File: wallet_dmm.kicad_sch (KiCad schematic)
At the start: 16 parts, among them J1 Conn_01x04, SW1 REST_BUTTON, U1 TLC555xD, U2 STM32L051K8Tx

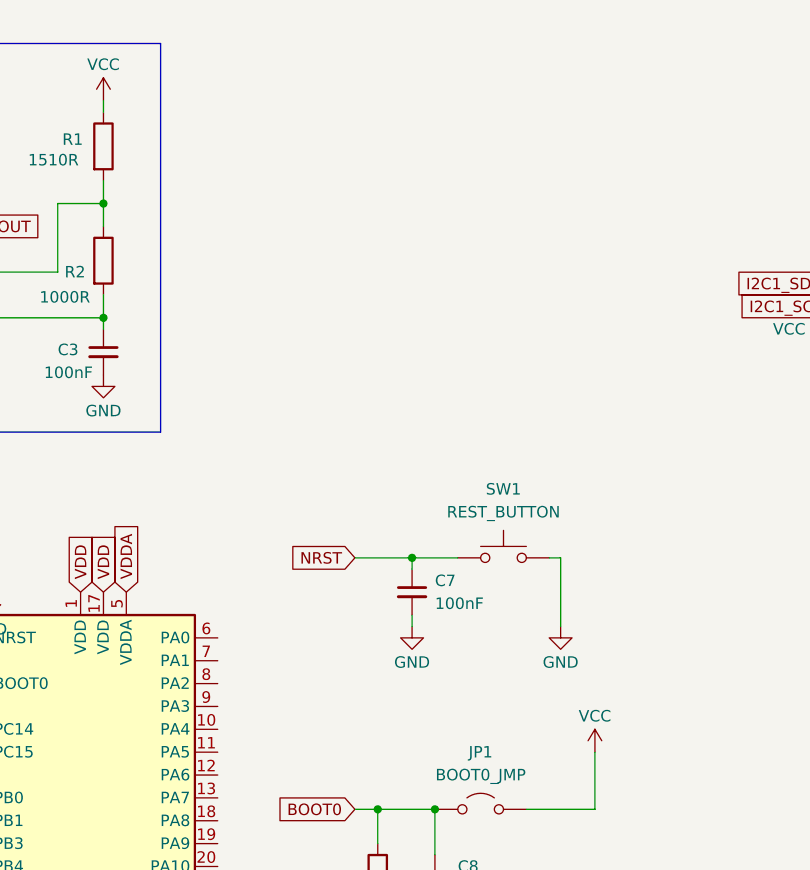
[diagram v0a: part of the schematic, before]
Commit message: Added temperature sensor to schematic and added .gitignore file.
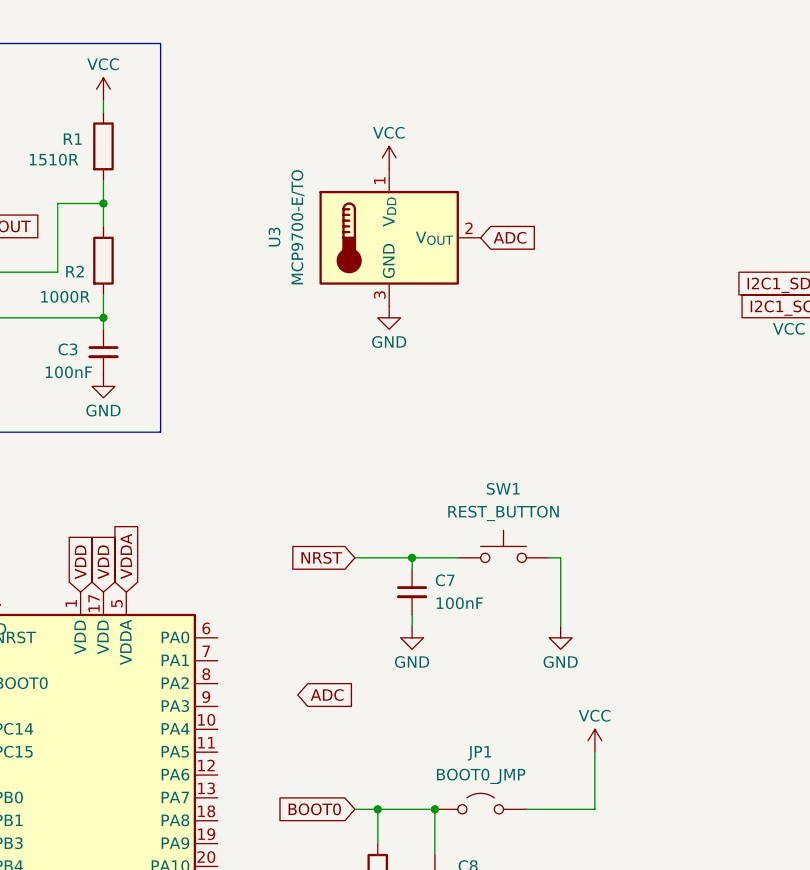
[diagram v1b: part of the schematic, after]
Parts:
- added U3: MCP9700-E/TO, footprints:TO-92_MC_MCH, symbol Sensor_Temperature:MCP9700Ax-ETT
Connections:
- net GND: now also U3.3 (GND)
- net VCC: now also U3.1 (V_{DD})
- new net ADC: U3.2 (V_{OUT})
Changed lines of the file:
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@@
+		)
+	)
+	(global_label "ADC"
+		(shape input)
+		(at 93.98 88.9 0)
+		(fields_autoplaced yes)
+		(effects
+			(font
+				(size 1.27 1.27)
+			)
+			(justify left)
+		)
+		(property "Intersheetrefs" "${INTERSHEET_REFS}"
+			(at 100.5938 88.9 0)
+			(effects
+				(font
+					(size 1.27 1.27)
+				)
+				(justify left)
+				(hide yes)
+			)
+		)
+	)
+	(global_label "ADC"
+		(shape input)
+		(at 114.3 38.1 0)
+		(fields_autoplaced yes)
+		(effects
+			(font
+				(size 1.27 1.27)
+			)
+			(justify left)
+		)
+		(property "Intersheetrefs" "${INTERSHEET_REFS}"
+			(at 120.9138 38.1 0)
+			(effects
+				(font
+					(size 1.27 1.27)
+				)
+				(justify left)
+				(hide yes)
+			)
 		)
 	)
@@
 	)
 	(symbol
+		(lib_id "power:VCC")
+		(at 104.14 30.48 0)
+		(mirror y)
+		(unit 1)
+		(exclude_from_sim no)
+		(in_bom yes)
+		(on_board yes)
+		(dnp no)
+		(property "Reference" "#PWR022"
+			(at 104.14 34.29 0)
+			(effects
+				(font
+					(size 1.27 1.27)
+				)
+				(hide yes)
+			)
+		)
+		(property "Value" "VCC"
+			(at 104.14 26.48 0)
+			(effects
+				(font
+					(size 1.27 1.27)
+				)
+			)
+		)
+		(property "Footprint" ""
+			(at 104.14 30.48 0)
+			(effects
+				(font
+					(size 1.27 1.27)
+				)
+				(hide yes)
+			)
+		)
+		(property "Datasheet" ""
+			(at 104.14 30.48 0)
+			(effects
+				(font
+					(size 1.27 1.27)
+				)
+				(hide yes)
+			)
+		)
+		(property "Description" "Power symbol creates a global label with name \"VCC\""
+			(at 104.14 30.48 0)
+			(effects
+				(font
+					(size 1.27 1.27)
+				)
+				(hide yes)
+			)
+		)
+		(pin "1"
+		)
+		(instances
+			(project "wallet_dmm"
+				(path "/2feb1339-af30-4942-92c0-e58400bfb20d"
+					(reference "#PWR022")
+					(unit 1)
+				)
+			)
+		)
+	)
+	(symbol
 		(lib_id "MCU_ST_STM32L0:STM32L051K8Tx")
 		(at 69.85 102.87 0)
@@
 	)
 	(symbol
+		(lib_id "Sensor_Temperature:MCP9700Ax-ETT")
+		(at 104.14 38.1 0)
+		(unit 1)
+		(exclude_from_sim no)
+		(in_bom yes)
+		(on_board yes)
+		(dnp no)
+		(property "Reference" "U3"
+			(at 91.44 36.83 90)
+			(effects
+				(font
+					(size 1.27 1.27)
+				)
+				(justify right)
+			)
+		)
+		(property "Value" "MCP9700-E/TO"
+			(at 93.98 30.48 90)
+			(effects
+				(font
+					(size 1.27 1.27)
+				)
+				(justify right)
+			)
+		)
+		(property "Footprint" "footprints:TO-92_MC_MCH"
+			(at 104.14 48.26 0)
+			(effects
+				(font
+					(size 1.27 1.27)
+				)
+				(hide yes)
+			)
+		)
+		(property "Datasheet" "http://ww1.microchip.com/downloads/en/devicedoc/20001942g.pdf"
+			(at 100.33 31.75 0)
+			(effects
+				(font
+					(size 1.27 1.27)
+				)
+				(hide yes)
+			)
+		)
+		(property "Description" "Low power, analog thermistor temperature sensor, ±2C accuracy, -40C to +125C, in SOT-23-3"
+			(at 104.14 38.1 0)
+			(effects
+				(font
+					(size 1.27 1.27)
+				)
+				(hide yes)
+			)
+		)
+		(pin "2"
+		)
+		(pin "3"
+		)
+		(pin "1"
+		)
+		(instances
+			(project "wallet_dmm"
+				(path "/2feb1339-af30-4942-92c0-e58400bfb20d"
+					(reference "U3")
+					(unit 1)
+				)
+			)
+		)
+	)
+	(symbol
 		(lib_id "Device:C_Small")
 		(at 34.29 80.01 0)
@@
 					(unit 1)
 				)
+			)
+		)
+	)
+	(symbol
+		(lib_id "power:GND")
+		(at 104.14 45.72 0)
+		(mirror y)
+		(unit 1)
+		(exclude_from_sim no)
+		(in_bom yes)
+		(on_board yes)
+		(dnp no)
+		(property "Reference" "#PWR023"
+			(at 104.14 52.07 0)
+			(effects
+				(font
+					(size 1.27 1.27)
+				)
+				(hide yes)
+			)
+		)
+		(property "Value" "GND"
+			(at 104.14 49.72 0)
+			(effects
+				(font
+					(size 1.27 1.27)
+				)
+			)
+		)
+		(property "Footprint" ""
+			(at 104.14 45.72 0)
+			(effects
+				(font
+					(size 1.27 1.27)
+				)
+				(hide yes)
+			)
+		)
+		(property "Datasheet" ""
+			(at 104.14 45.72 0)
+			(effects
+				(font
+					(size 1.27 1.27)
+				)
+				(hide yes)
+			)
+		)
+		(property "Description" "Power symbol creates a global label with name \"GND\" , ground"
+			(at 104.14 45.72 0)
+			(effects
+				(font
+					(size 1.27 1.27)
+				)
+				(hide yes)
+			)
+		)
+		(pin "1"
+		)
+		(instances
+			(project "wallet_dmm"
+				(path "/2feb1339-af30-4942-92c0-e58400bfb20d"
+					(reference "#PWR023")
+					(unit 1)
+				)

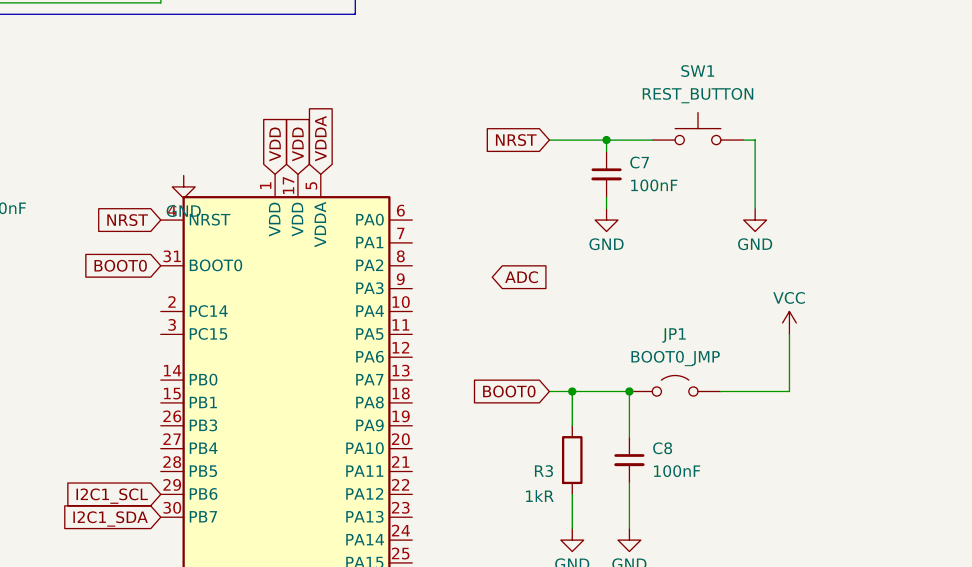
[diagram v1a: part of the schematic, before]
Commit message: Added OLED footprint
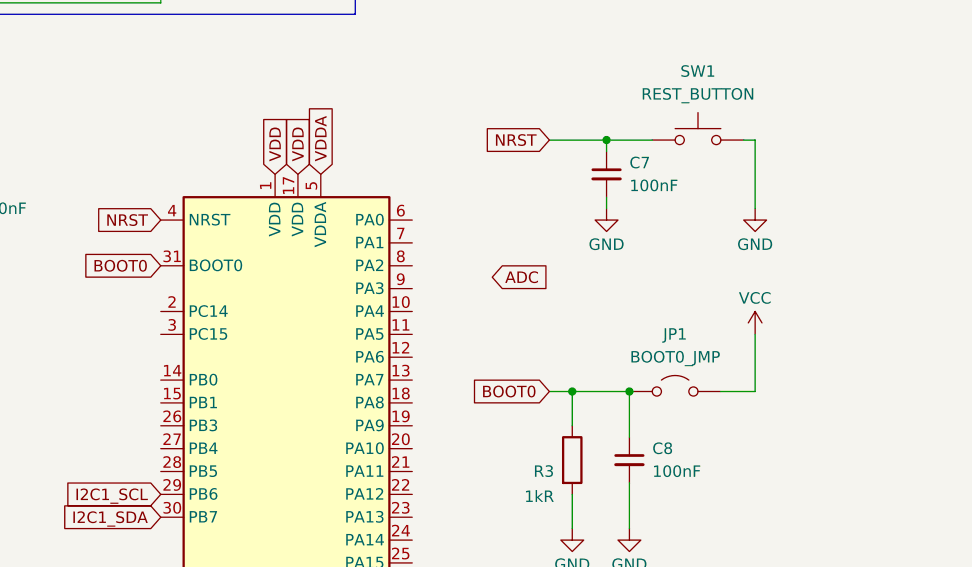
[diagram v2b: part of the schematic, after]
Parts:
- J1: footprint (none) -> project_specific:OLED_Header
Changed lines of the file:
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@@
 	(wire
 		(pts
-			(xy 119.38 101.6) (xy 127 101.6)
+			(xy 119.38 101.6) (xy 123.19 101.6)
 		)
 		(stroke
@@
 	(wire
 		(pts
-			(xy 127 101.6) (xy 127 95.25)
+			(xy 123.19 101.6) (xy 123.19 95.25)
 		)
 		(stroke
@@
 	)
 	(symbol
-		(lib_id "power:GND")
-		(at 59.6977 77.5991 0)
-		(mirror y)
-		(unit 1)
-		(exclude_from_sim no)
-		(in_bom yes)
-		(on_board yes)
-		(dnp no)
-		(property "Reference" "#PWR020"
-			(at 59.6977 83.9491 0)
-			(effects
-				(font
-					(size 1.27 1.27)
-				)
-				(hide yes)
-			)
-		)
-		(property "Value" "GND"
-			(at 59.6977 81.5991 0)
-			(effects
-				(font
-					(size 1.27 1.27)
-				)
-			)
-		)
-		(property "Footprint" ""
-			(at 59.6977 77.5991 0)
-			(effects
-				(font
-					(size 1.27 1.27)
-				)
-				(hide yes)
-			)
-		)
-		(property "Datasheet" ""
-			(at 59.6977 77.5991 0)
-			(effects
-				(font
-					(size 1.27 1.27)
-				)
-				(hide yes)
-			)
-		)
-		(property "Description" "Power symbol creates a global label with name \"GND\" , ground"
-			(at 59.6977 77.5991 0)
-			(effects
-				(font
-					(size 1.27 1.27)
-				)
-				(hide yes)
-			)
-		)
-		(pin "1"
-		)
-		(instances
-			(project "wallet_dmm"
-				(path "/2feb1339-af30-4942-92c0-e58400bfb20d"
-					(reference "#PWR020")
-					(unit 1)
-				)
-			)
-		)
-	)
-	(symbol
 		(lib_id "Device:C_Small")
 		(at 106.68 77.47 0)
@@
 	(symbol
 		(lib_id "power:VCC")
-		(at 127 95.25 0)
+		(at 123.19 95.25 0)
 		(mirror y)
 		(unit 1)
@@
 		(dnp no)
 		(property "Reference" "#PWR021"
-			(at 127 99.06 0)
+			(at 123.19 99.06 0)
 			(effects
 				(font
@@
 		)
 		(property "Value" "VCC"
-			(at 127 91.25 0)
+			(at 123.19 91.25 0)
 			(effects
 				(font
@@
 		)
 		(property "Footprint" ""
-			(at 127 95.25 0)
+			(at 123.19 95.25 0)
 			(effects
 				(font
@@
 		)
 		(property "Datasheet" ""
-			(at 127 95.25 0)
+			(at 123.19 95.25 0)
 			(effects
 				(font
@@
 		)
 		(property "Description" "Power symbol creates a global label with name \"VCC\""
-			(at 127 95.25 0)
+			(at 123.19 95.25 0)
 			(effects
 				(font
@@
 			)
 		)
-		(property "Footprint" ""
+		(property "Footprint" "project_specific:OLED_Header"
 			(at 158.75 45.72 0)
 			(effects

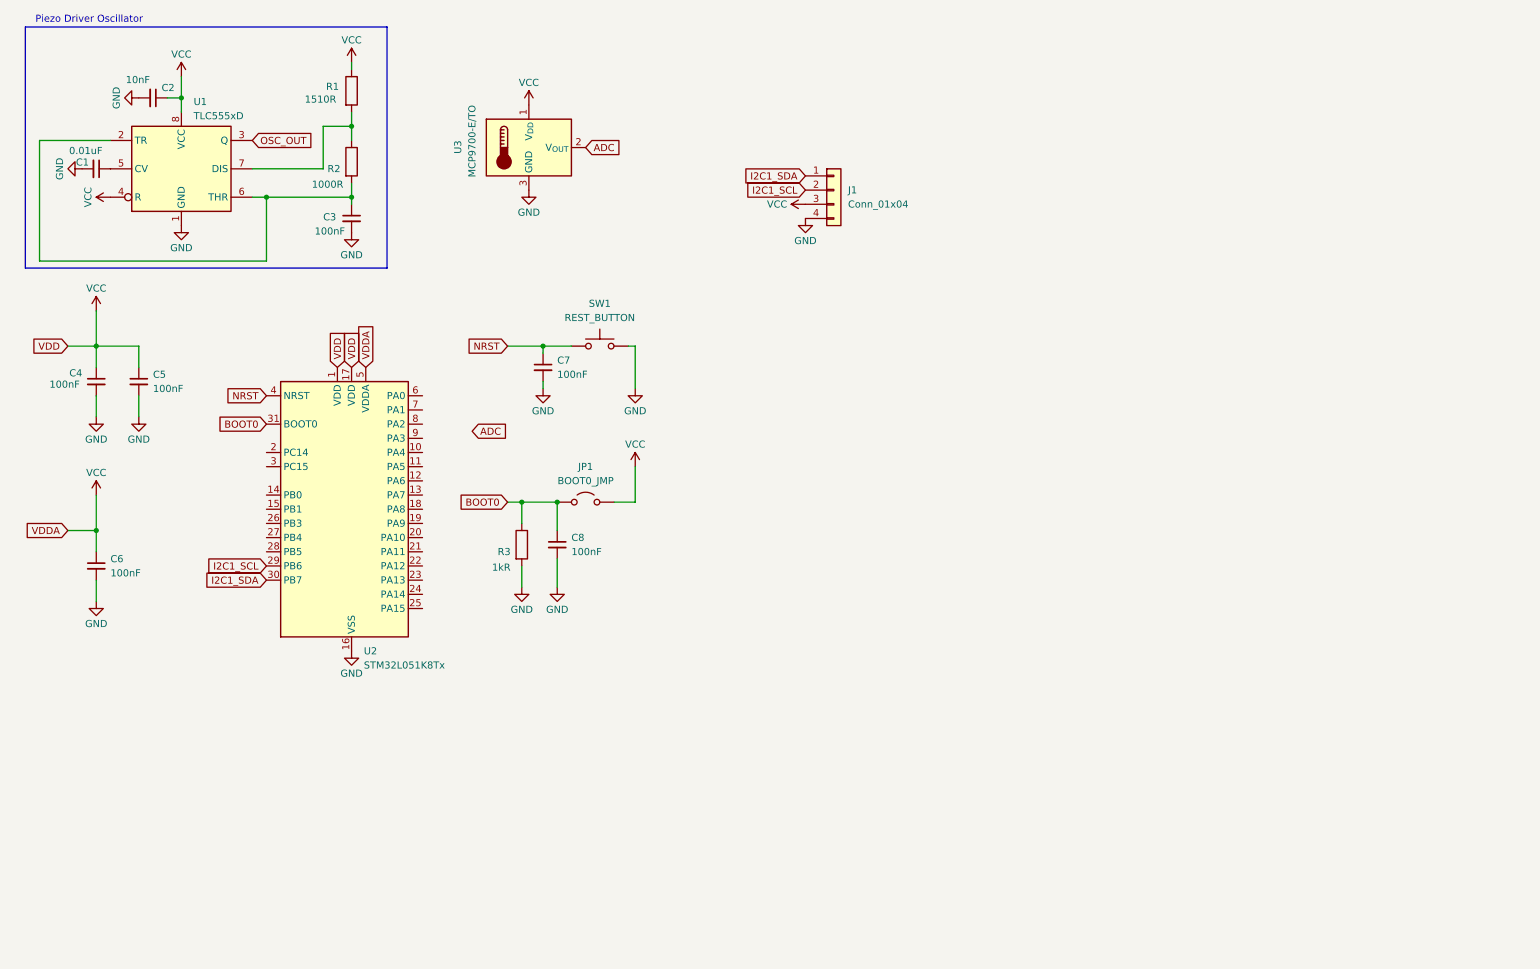
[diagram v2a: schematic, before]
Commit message: Added piezo buzzer and control circuitry.
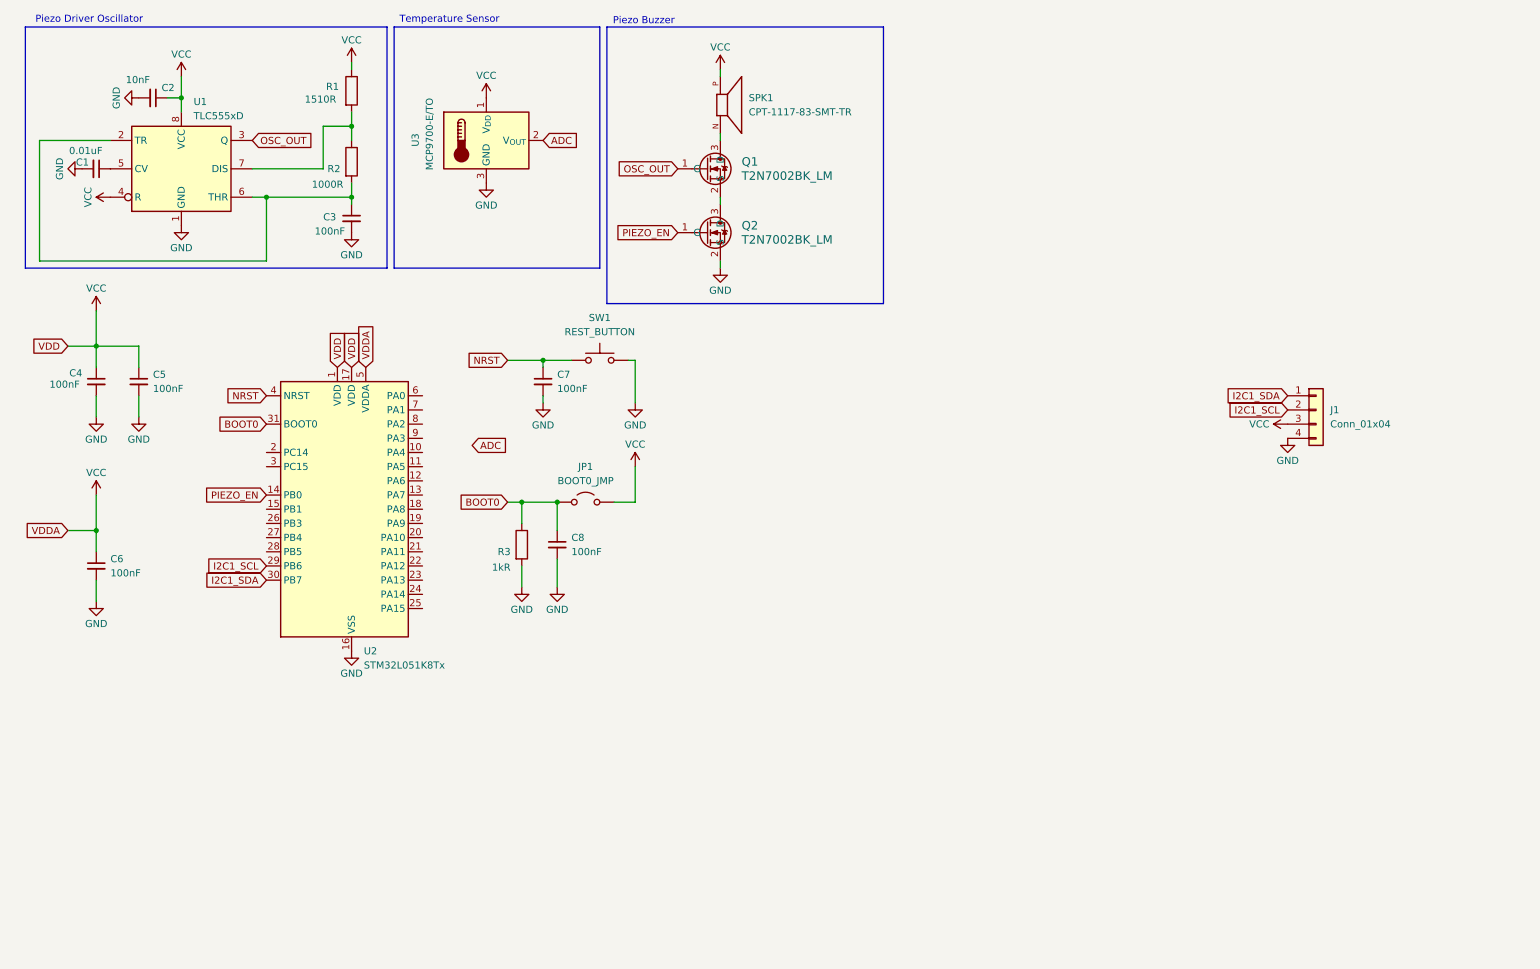
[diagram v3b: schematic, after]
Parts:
- added Q1, Q2: T2N7002BK_LM, T2N7002BK:SOT23_TOS, symbol T2N7002BK:T2N7002BK_LM
- added SPK1: CPT-1117-83-SMT-TR, wallet_dmm:XDCR_CPT-1117-83-SMT-TR, symbol CPT-1117-83-SMT-TR:CPT-1117-83-SMT-TR
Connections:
- net GND: now also Q2.2 (S)
- net OSC_OUT: now also Q1.1 (G)
- net VCC: now also SPK1.P
- net PIEZO_EN: now reaches U2.14 (PB0)
- net PIEZO_EN: now also Q2.1 (G)
- new net: Q1.3 (D), SPK1.N
- new net: Q1.2 (S), Q2.3 (D)
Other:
- note added: "Piezo Buzzer"
- note added: "Temperature Sensor"
- moved on the sheet: C7, J1, SW1, U3
